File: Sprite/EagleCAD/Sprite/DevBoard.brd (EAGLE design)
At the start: 35 x 35 mm, 30 parts, among them U1 CC430F5137, U2 HMC5883LSMD, U3 ITG-3200, X1 26 MHz

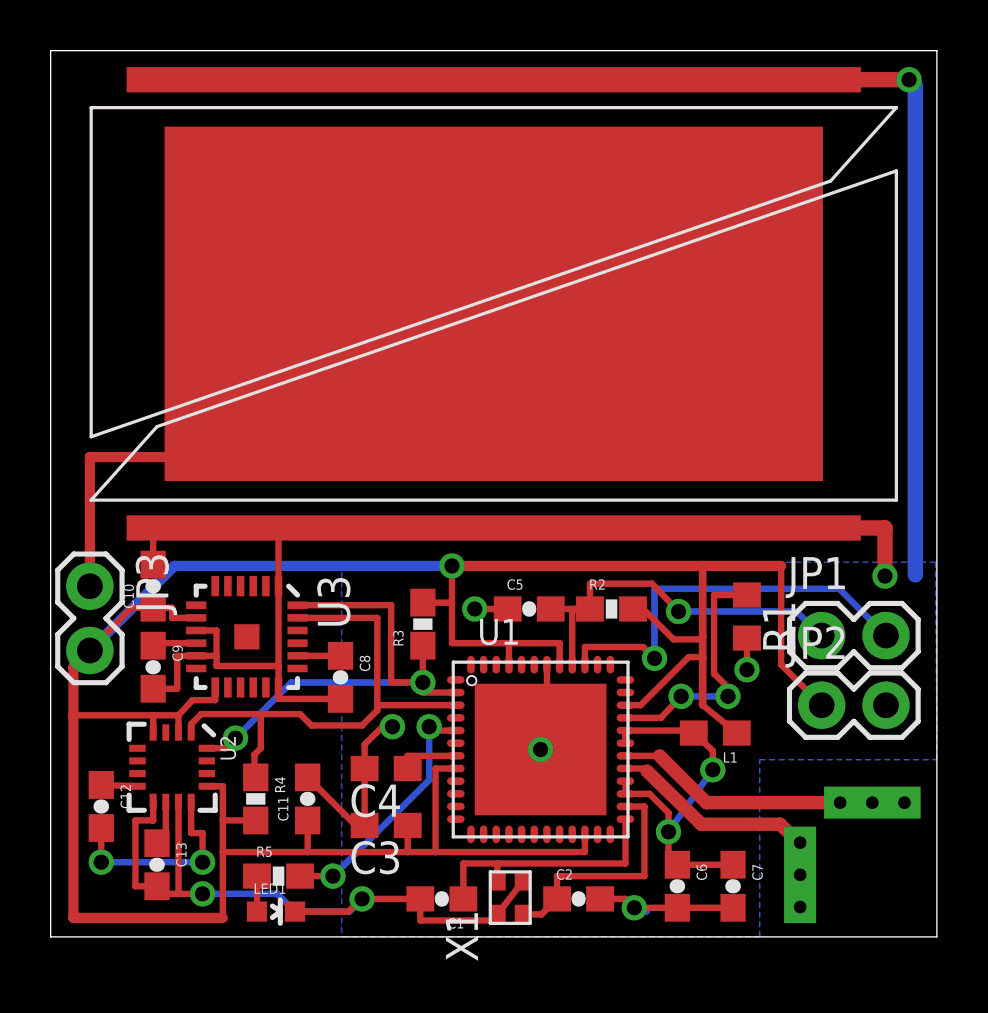
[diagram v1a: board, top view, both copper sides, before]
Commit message: Added headers for serial port
Put an extra pair of headers on the board to interface with a serial
port for Energia debugging.  Still have to figure out which MCU pins to
use
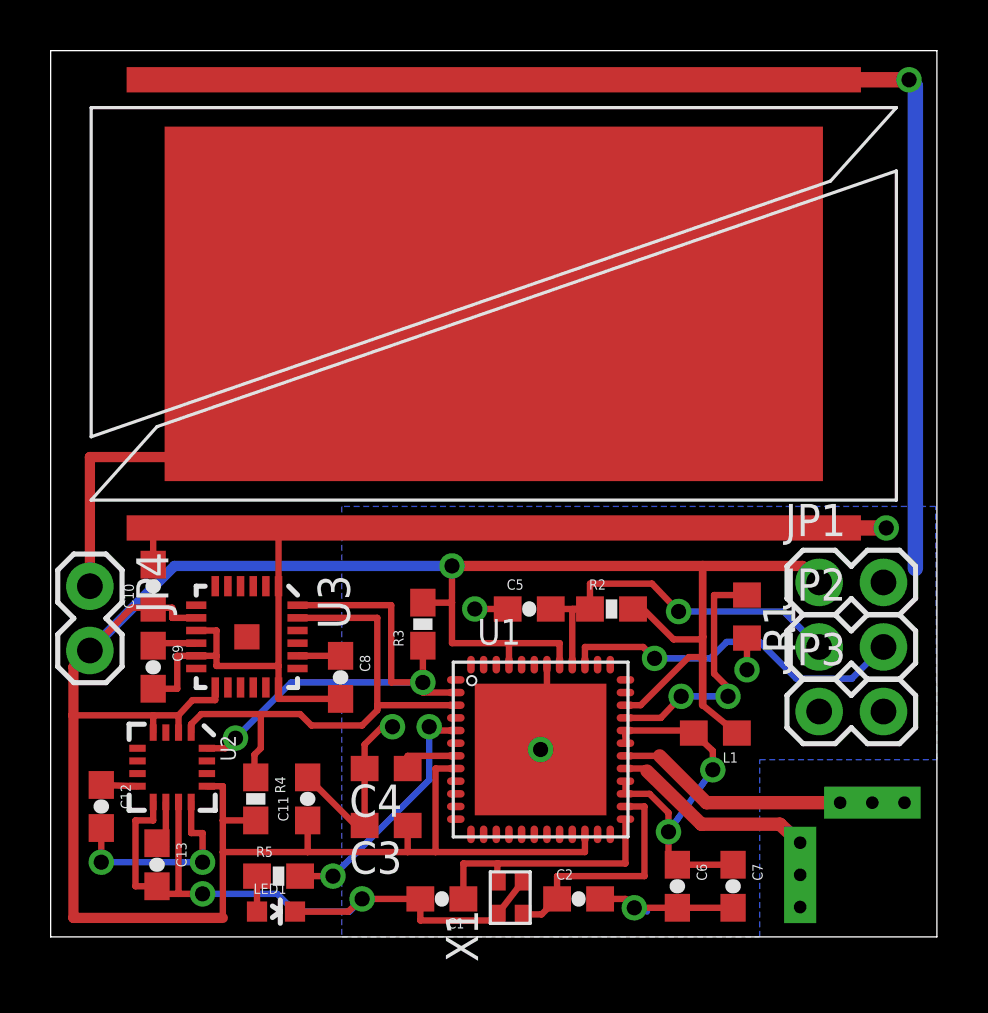
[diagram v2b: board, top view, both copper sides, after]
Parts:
- added JP4: (no value), SparkFun:1X02
- moved JP3 29.2 mm to (30.4, 8.90), turned to 0 degrees
- moved JP2 2.30 mm to (30.4, 11.4)
- moved JP1 2.10 mm to (30.4, 14.0)
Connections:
- net GND: now also JP1.2; no longer JP2.2
- net RST: now also JP2.1; no longer JP1.1
- net TEST: now also JP2.2; no longer JP1.2
- net VCC: now also JP1.1, JP4.2; no longer JP2.1, JP3.2
- net VSOLAR: now also JP4.1; no longer JP3.1
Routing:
- net VCC: track 117.7 -> 113.3 mm
- net TEST: track 16.3 -> 14.1 mm
- net GND: track 156.3 -> 154.2 mm
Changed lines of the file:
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@@
 <element name="R3" library="SparkFun" package="0603-RES" value="4.7K" x="14.7" y="12.35" rot="R90"/>
 <element name="R4" library="SparkFun" package="0603-RES" value="4.7K" x="8.1" y="5.45" rot="R270"/>
-<element name="JP1" library="SparkFun" package="1X02" value="" x="30.45" y="11.9"/>
-<element name="JP2" library="SparkFun" package="1X02" value="" x="30.45" y="9.15"/>
+<element name="JP2" library="SparkFun" package="1X02" value="" x="30.35" y="11.45"/>
+<element name="JP1" library="SparkFun" package="1X02" value="" x="30.35" y="14"/>
 <element name="ANT-N" library="SpriteAntenna" package="ANTENNA" value="ANTENNA" x="32.45" y="5.3" rot="R180"/>
 <element name="ANT-P" library="SpriteAntenna" package="ANTENNA" value="ANTENNA" x="29.6" y="2.45" rot="R90"/>
@@
 <element name="R5" library="SparkFun" package="0603-RES" value="270R" x="9" y="2.4"/>
 <element name="X1" library="ABM11" package="ABM11_CERAMIC-SMD-CRYSTAL" value="26 MHz" x="18.15" y="1.55" rot="R90"/>
-<element name="JP3" library="SparkFun" package="1X02" value="" x="1.55" y="13.85" rot="R270"/>
+<element name="JP4" library="SparkFun" package="1X02" value="" x="1.55" y="13.85" rot="R270"/>
+<element name="JP3" library="SparkFun" package="1X02" value="" x="30.35" y="8.9"/>
 </elements>
 <signals>
@@
 <contactref element="R3" pad="2"/>
 <contactref element="R4" pad="2"/>
-<wire x1="28.85" y1="14.65" x2="25.75" y2="14.65" width="0.4064" layer="1"/>
+<wire x1="29.7" y1="14.65" x2="25.75" y2="14.65" width="0.4064" layer="1"/>
 <wire x1="25.75" y1="14.65" x2="15.85" y2="14.65" width="0.4064" layer="1"/>
 <wire x1="0.9" y1="8.75" x2="0.9" y2="0.75" width="0.4064" layer="1"/>
@@
 <wire x1="4.05" y1="8.75" x2="0.9" y2="8.75" width="0.254" layer="1"/>
 <wire x1="6.5" y1="9.85" x2="6.5" y2="9.35" width="0.254" layer="1"/>
-<contactref element="JP2" pad="1"/>
+<contactref element="JP1" pad="1"/>
 <wire x1="8.1" y1="4.6" x2="6.8" y2="4.6" width="0.254" layer="1"/>
 <contactref element="U3" pad="8"/>
@@
 <wire x1="18.1" y1="11.6" x2="15.85" y2="11.6" width="0.254" layer="1"/>
 <wire x1="15.85" y1="11.6" x2="15.85" y2="13.2" width="0.254" layer="1"/>
-<wire x1="15.85" y1="13.25" x2="15.85" y2="14.65" width="0.254" layer="1"/>
+<wire x1="15.85" y1="13.2" x2="15.85" y2="14.65" width="0.254" layer="1"/>
 <wire x1="20.1" y1="10.75" x2="20.1" y2="11.6" width="0.254" layer="1"/>
 <wire x1="20.1" y1="11.6" x2="18.1" y2="11.6" width="0.254" layer="1"/>
@@
 <wire x1="10.15" y1="3.35" x2="10.15" y2="4.6" width="0.254" layer="1"/>
 <wire x1="14.1" y1="3.35" x2="10.15" y2="3.35" width="0.254" layer="1"/>
-<wire x1="30.45" y1="9.15" x2="28.85" y2="10.75" width="0.254" layer="1"/>
-<wire x1="28.85" y1="10.75" x2="28.85" y2="14.65" width="0.254" layer="1"/>
 <wire x1="23.4" y1="12.95" x2="24.6" y2="11.75" width="0.254" layer="1"/>
 <contactref element="L1" pad="1"/>
@@
 <wire x1="24.6" y1="11.75" x2="25.65" y2="11.75" width="0.254" layer="1"/>
 <wire x1="25.65" y1="11.75" x2="25.75" y2="11.85" width="0.254" layer="1"/>
-<contactref element="JP3" pad="2"/>
+<contactref element="JP4" pad="2"/>
 <wire x1="0.9" y1="8.75" x2="0.9" y2="10.66" width="0.4064" layer="1"/>
 <wire x1="0.9" y1="10.66" x2="1.55" y2="11.31" width="0.4064" layer="1"/>
@@
 <wire x1="4.89" y1="14.65" x2="1.55" y2="11.31" width="0.4064" layer="16"/>
 <wire x1="14.7" y1="13.2" x2="15.85" y2="13.2" width="0.254" layer="1"/>
-<wire x1="15.85" y1="13.2" x2="15.85" y2="13.25" width="0.254" layer="1"/>
+<wire x1="29.7" y1="14.65" x2="30.35" y2="14" width="0.4064" layer="1"/>
 </signal>
 <signal name="GND">
@@
 <contactref element="U3" pad="1"/>
 <polygon width="0.4064" layer="16">
-<vertex x="11.5" y="14.8"/>
+<vertex x="11.5" y="17"/>
 <vertex x="11.5" y="0"/>
 <vertex x="28" y="0"/>
 <vertex x="28" y="7"/>
 <vertex x="35" y="7"/>
-<vertex x="34.95" y="14.8"/>
+<vertex x="34.95" y="17"/>
 </polygon>
-<via x="32.95" y="14.25" extent="1-16" drill="0.6"/>
+<via x="33" y="16.15" extent="1-16" drill="0.6"/>
 <via x="27.5" y="10.55" extent="1-16" drill="0.6"/>
 <wire x1="12.4" y1="4.4" x2="12.4" y2="6.65" width="0.254" layer="1"/>
@@
 <wire x1="9" y1="9.4" x2="11.45" y2="9.4" width="0.254" layer="1"/>
 <wire x1="9" y1="9.85" x2="9" y2="10.7" width="0.254" layer="1"/>
-<contactref element="JP2" pad="2"/>
+<contactref element="JP1" pad="2"/>
 <wire x1="9" y1="10.7" x2="9" y2="13.85" width="0.254" layer="1"/>
 <wire x1="5.75" y1="11.1" x2="5" y2="11.1" width="0.254" layer="1"/>
@@
 <wire x1="17.5" y1="33.85" x2="33.9" y2="33.85" width="0.6096" layer="1"/>
 <via x="33.9" y="33.85" extent="1-16" drill="0.6"/>
-<wire x1="34.15" y1="14.3" x2="34.15" y2="33.6" width="0.6096" layer="16"/>
+<wire x1="34.15" y1="14.55" x2="34.15" y2="33.6" width="0.6096" layer="16"/>
 <wire x1="34.15" y1="33.6" x2="33.9" y2="33.85" width="0.6096" layer="16"/>
 <contactref element="LED1" pad="C"/>
@@
 <wire x1="4.05" y1="16.15" x2="9" y2="16.15" width="0.254" layer="1"/>
 <wire x1="9" y1="16.15" x2="9" y2="16.05" width="0.254" layer="1"/>
-<wire x1="32.95" y1="16.15" x2="32.95" y2="14.25" width="0.6096" layer="1"/>
+<wire x1="32.95" y1="16.15" x2="33" y2="16.15" width="0.6096" layer="1"/>
+<wire x1="32.89" y1="14" x2="34.15" y2="14.55" width="0" layer="19" extent="16-16"/>
 </signal>
 <signal name="N$1">
@@
 <signal name="RST">
 <contactref element="U1" pad="40"/>
-<contactref element="JP1" pad="1"/>
+<contactref element="JP2" pad="1"/>
 <via x="24.8" y="12.85" extent="1-16" drill="0.6"/>
 <contactref element="R2" pad="1"/>
@@
 <wire x1="21.3" y1="13.95" x2="23.75" y2="13.95" width="0.254" layer="1"/>
 <wire x1="23.75" y1="13.95" x2="24.8" y2="12.85" width="0.254" layer="1"/>
-<wire x1="24.8" y1="12.85" x2="29.45" y2="12.85" width="0.254" layer="16"/>
-<wire x1="29.45" y1="12.85" x2="30.45" y2="11.9" width="0.254" layer="16"/>
+<wire x1="24.8" y1="12.85" x2="28.95" y2="12.85" width="0.254" layer="16"/>
+<wire x1="28.95" y1="12.85" x2="30.35" y2="11.45" width="0.254" layer="16"/>
 </signal>
 <signal name="TEST">
 <contactref element="U1" pad="39"/>
-<contactref element="JP1" pad="2"/>
+<contactref element="JP2" pad="2"/>
 <via x="23.85" y="11" extent="1-16" drill="0.6"/>
-<wire x1="23.85" y1="11" x2="23.85" y2="13.75" width="0.254" layer="16"/>
-<wire x1="23.85" y1="13.75" x2="31.14" y2="13.75" width="0.254" layer="16"/>
-<wire x1="31.14" y1="13.75" x2="32.99" y2="11.9" width="0.254" layer="16"/>
 <wire x1="21.1" y1="10.75" x2="21.1" y2="11.45" width="0.254" layer="1"/>
 <wire x1="21.1" y1="11.45" x2="23.4" y2="11.45" width="0.254" layer="1"/>
 <wire x1="23.4" y1="11.45" x2="23.85" y2="11" width="0.254" layer="1"/>
+<wire x1="23.85" y1="11" x2="26.05" y2="11" width="0.254" layer="16"/>
+<wire x1="26.05" y1="11" x2="26.7" y2="11.65" width="0.254" layer="16"/>
+<wire x1="26.7" y1="11.65" x2="28" y2="11.65" width="0.254" layer="16"/>
+<wire x1="28" y1="11.65" x2="29.45" y2="10.2" width="0.254" layer="16"/>
+<wire x1="29.45" y1="10.2" x2="31.64" y2="10.2" width="0.254" layer="16"/>
+<wire x1="31.64" y1="10.2" x2="32.89" y2="11.45" width="0.254" layer="16"/>
 </signal>
 <signal name="SCL">
@@
 </signal>
 <signal name="VSOLAR">
-<contactref element="JP3" pad="1"/>
+<contactref element="JP4" pad="1"/>
 <contactref element="S1" pad="PLUS"/>
 <wire x1="1.55" y1="13.85" x2="1.55" y2="18.95" width="0.4064" layer="1"/>
